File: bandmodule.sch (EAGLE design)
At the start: 15 parts

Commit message: Readme, made more space for toroids
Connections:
- net GND: now also C12.1; no longer C12.2
- net N$6: now also C12.2; no longer C12.1
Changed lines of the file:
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@@
 </segment>
 <segment>
-<pinref part="C12" gate="G$1" pin="2"/>
+<pinref part="C12" gate="G$1" pin="1"/>
 <pinref part="GND8" gate="1" pin="GND"/>
-<wire x1="66.04" y1="22.86" x2="66.04" y2="12.7" width="0.1524" layer="91"/>
+<wire x1="66.04" y1="15.24" x2="66.04" y2="12.7" width="0.1524" layer="91"/>
 </segment>
 </net>
@@
 <segment>
 <pinref part="L7" gate="G$1" pin="1"/>
-<pinref part="C12" gate="G$1" pin="1"/>
+<pinref part="C12" gate="G$1" pin="2"/>
 <wire x1="50.8" y1="27.94" x2="66.04" y2="27.94" width="0.1524" layer="91"/>
 <wire x1="66.04" y1="27.94" x2="66.04" y2="25.4" width="0.1524" layer="91"/>
 <pinref part="TXIN" gate="-2" pin="S"/>
-<wire x1="66.04" y1="25.4" x2="66.04" y2="15.24" width="0.1524" layer="91"/>
+<wire x1="66.04" y1="25.4" x2="66.04" y2="22.86" width="0.1524" layer="91"/>
 <wire x1="66.04" y1="25.4" x2="71.12" y2="25.4" width="0.1524" layer="91"/>
 <junction x="66.04" y="25.4"/>

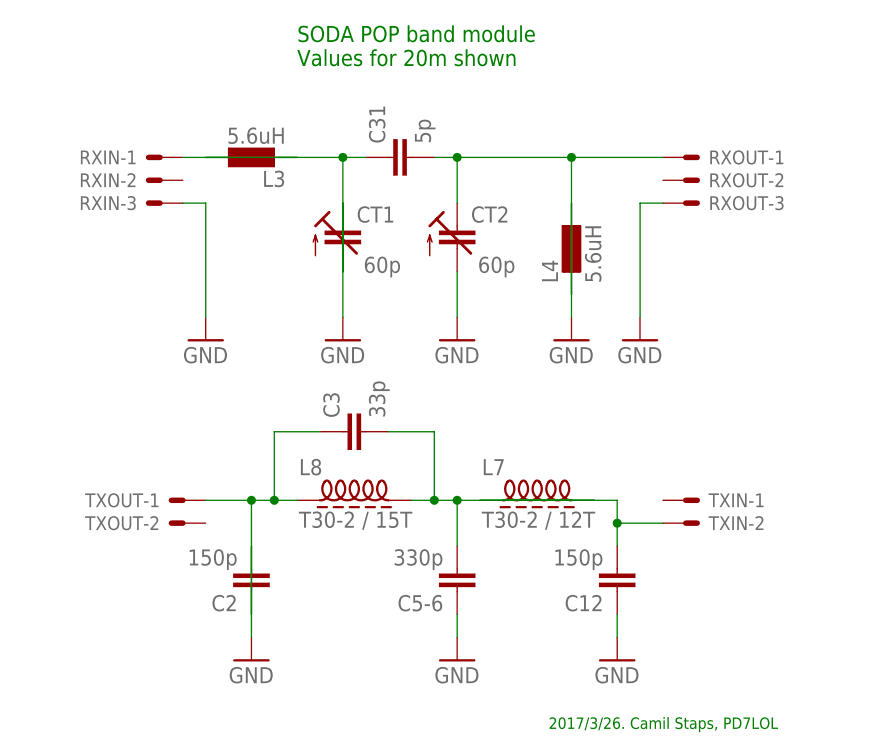
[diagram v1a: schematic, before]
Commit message: Move labels, add white rectangle for band
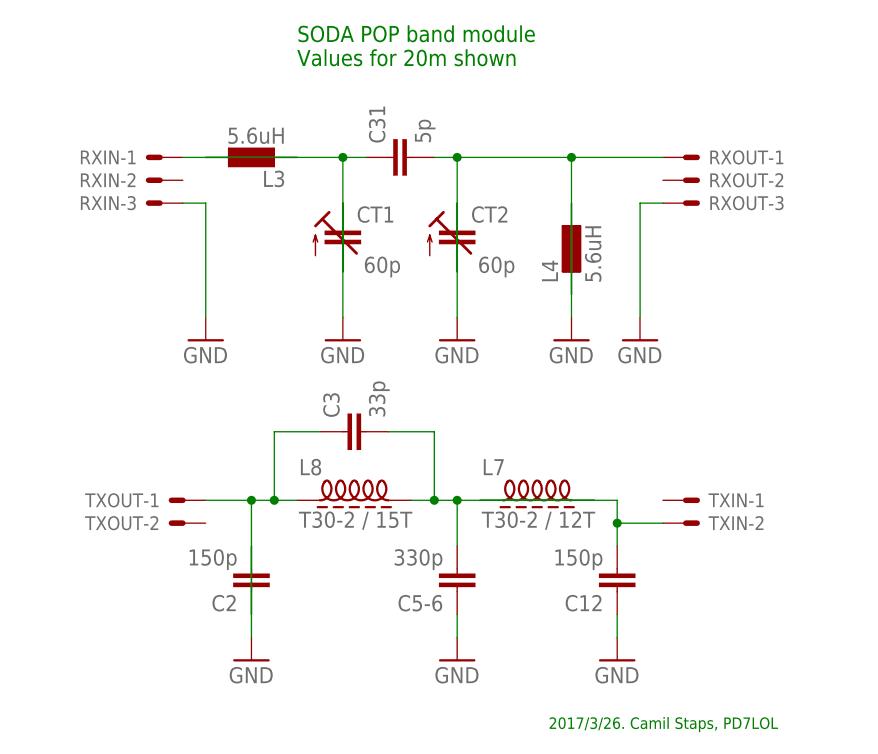
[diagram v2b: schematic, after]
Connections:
- net GND: now also CT2.E; no longer CT2.A
- net N$4: now also CT2.A; no longer CT2.E
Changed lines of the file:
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@@
 <grid distance="0.1" unitdist="inch" unit="inch" style="lines" multiple="1" display="no" altdistance="0.01" altunitdist="inch" altunit="inch"/>
 <layers>
-<layer number="1" name="Top" color="4" fill="10" visible="yes" active="no"/>
-<layer number="16" name="Bottom" color="1" fill="1" visible="yes" active="no"/>
-<layer number="17" name="Pads" color="2" fill="1" visible="yes" active="no"/>
-<layer number="18" name="Vias" color="2" fill="1" visible="yes" active="no"/>
-<layer number="19" name="Unrouted" color="6" fill="1" visible="yes" active="no"/>
-<layer number="20" name="Dimension" color="15" fill="1" visible="yes" active="no"/>
-<layer number="21" name="tPlace" color="7" fill="1" visible="yes" active="no"/>
-<layer number="22" name="bPlace" color="7" fill="1" visible="yes" active="no"/>
-<layer number="23" name="tOrigins" color="15" fill="1" visible="yes" active="no"/>
-<layer number="24" name="bOrigins" color="15" fill="1" visible="yes" active="no"/>
-<layer number="25" name="tNames" color="7" fill="1" visible="yes" active="no"/>
-<layer number="26" name="bNames" color="7" fill="1" visible="yes" active="no"/>
-<layer number="27" name="tValues" color="7" fill="1" visible="yes" active="no"/>
-<layer number="28" name="bValues" color="7" fill="1" visible="yes" active="no"/>
+<layer number="1" name="Top" color="4" fill="10" visible="no" active="no"/>
+<layer number="16" name="Bottom" color="1" fill="1" visible="no" active="no"/>
+<layer number="17" name="Pads" color="2" fill="1" visible="no" active="no"/>
+<layer number="18" name="Vias" color="2" fill="1" visible="no" active="no"/>
+<layer number="19" name="Unrouted" color="6" fill="1" visible="no" active="no"/>
+<layer number="20" name="Dimension" color="15" fill="1" visible="no" active="no"/>
+<layer number="21" name="tPlace" color="7" fill="1" visible="no" active="no"/>
+<layer number="22" name="bPlace" color="7" fill="1" visible="no" active="no"/>
+<layer number="23" name="tOrigins" color="15" fill="1" visible="no" active="no"/>
+<layer number="24" name="bOrigins" color="15" fill="1" visible="no" active="no"/>
+<layer number="25" name="tNames" color="7" fill="1" visible="no" active="no"/>
+<layer number="26" name="bNames" color="7" fill="1" visible="no" active="no"/>
+<layer number="27" name="tValues" color="7" fill="1" visible="no" active="no"/>
+<layer number="28" name="bValues" color="7" fill="1" visible="no" active="no"/>
 <layer number="29" name="tStop" color="7" fill="3" visible="no" active="no"/>
 <layer number="30" name="bStop" color="7" fill="6" visible="no" active="no"/>
@@
 <layer number="35" name="tGlue" color="7" fill="4" visible="no" active="no"/>
 <layer number="36" name="bGlue" color="7" fill="5" visible="no" active="no"/>
-<layer number="37" name="tTest" color="7" fill="1" visible="yes" active="no"/>
-<layer number="38" name="bTest" color="7" fill="1" visible="yes" active="no"/>
+<layer number="37" name="tTest" color="7" fill="1" visible="no" active="no"/>
+<layer number="38" name="bTest" color="7" fill="1" visible="no" active="no"/>
 <layer number="39" name="tKeepout" color="4" fill="11" visible="no" active="no"/>
 <layer number="40" name="bKeepout" color="1" fill="11" visible="no" active="no"/>
@@
 <layer number="44" name="Drills" color="7" fill="1" visible="no" active="no"/>
 <layer number="45" name="Holes" color="7" fill="1" visible="no" active="no"/>
-<layer number="46" name="Milling" color="3" fill="1" visible="yes" active="no"/>
-<layer number="47" name="Measures" color="7" fill="1" visible="yes" active="no"/>
-<layer number="48" name="Document" color="7" fill="1" visible="yes" active="no"/>
-<layer number="49" name="Reference" color="7" fill="1" visible="yes" active="no"/>
-<layer number="51" name="tDocu" color="26" fill="1" visible="yes" active="no"/>
-<layer number="52" name="bDocu" color="7" fill="1" visible="yes" active="no"/>
+<layer number="46" name="Milling" color="3" fill="1" visible="no" active="no"/>
+<layer number="47" name="Measures" color="7" fill="1" visible="no" active="no"/>
+<layer number="48" name="Document" color="7" fill="1" visible="no" active="no"/>
+<layer number="49" name="Reference" color="7" fill="1" visible="no" active="no"/>
+<layer number="51" name="tDocu" color="26" fill="1" visible="no" active="no"/>
+<layer number="52" name="bDocu" color="7" fill="1" visible="no" active="no"/>
 <layer number="90" name="Modules" color="5" fill="1" visible="yes" active="yes"/>
 <layer number="91" name="Nets" color="2" fill="1" visible="yes" active="yes"/>
@@
 <pinref part="C31" gate="G$1" pin="2"/>
 <wire x1="45.72" y1="66.04" x2="48.26" y2="66.04" width="0.1524" layer="91"/>
-<pinref part="CT2" gate="G$1" pin="E"/>
+<pinref part="CT2" gate="G$1" pin="A"/>
 <wire x1="48.26" y1="66.04" x2="60.96" y2="66.04" width="0.1524" layer="91"/>
-<wire x1="48.26" y1="66.04" x2="48.26" y2="60.96" width="0.1524" layer="91"/>
+<wire x1="48.26" y1="66.04" x2="48.26" y2="53.34" width="0.1524" layer="91"/>
 <junction x="48.26" y="66.04"/>
 <junction x="60.96" y="66.04"/>
@@
 </segment>
 <segment>
-<pinref part="CT2" gate="G$1" pin="A"/>
+<pinref part="CT2" gate="G$1" pin="E"/>
 <pinref part="GND4" gate="1" pin="GND"/>
-<wire x1="48.26" y1="53.34" x2="48.26" y2="48.26" width="0.1524" layer="91"/>
+<wire x1="48.26" y1="60.96" x2="48.26" y2="48.26" width="0.1524" layer="91"/>
 </segment>
 <segment>

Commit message: Split up C5-6
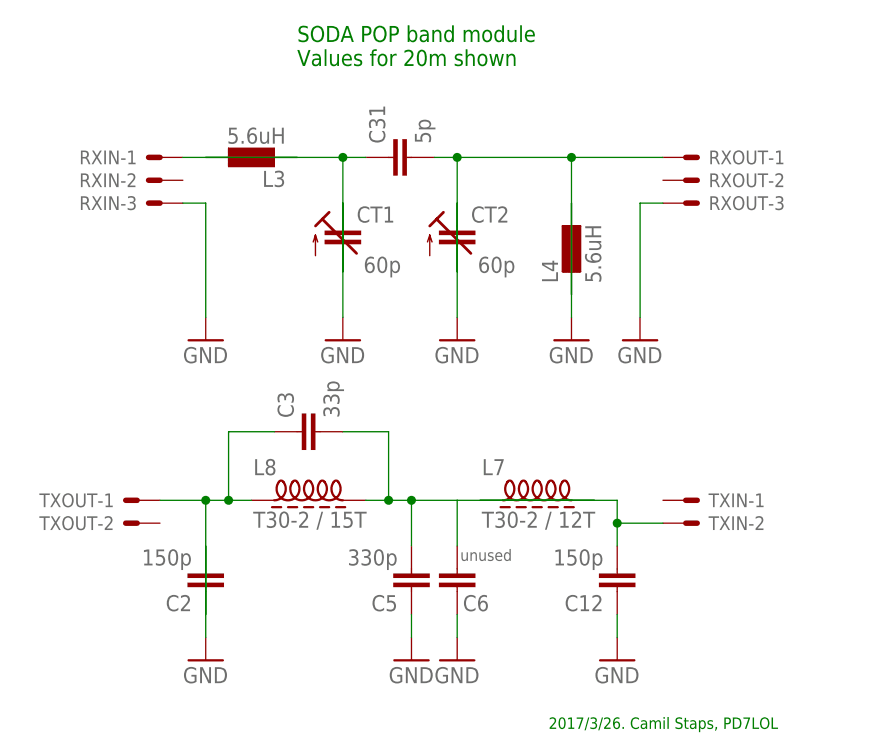
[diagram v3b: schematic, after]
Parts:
- added C5: 330p, capacitor-wima:C5/2.5
- C6: value 330p -> unused
- renumbered C5-6 to C6
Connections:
- net GND: now also C5.1
- net N$5: now also C5.2
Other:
- moved on the sheet: C2, C3, L8, TXOUT-1, TXOUT-2
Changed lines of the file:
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@@
 <part name="L8" library="toroids" deviceset="INDUCTOR" device="T30-2-28AWG-12T" value="T30-2 / 15T"/>
 <part name="L7" library="toroids" deviceset="INDUCTOR" device="T30-2-28AWG-12T" value="T30-2 / 12T"/>
-<part name="C5-6" library="capacitor-wima" deviceset="C" device="5/2.5" value="330p"/>
+<part name="C5" library="capacitor-wima" deviceset="C" device="5/2.5" value="330p"/>
 <part name="C12" library="capacitor-wima" deviceset="C" device="5/2.5" value="150p"/>
 <part name="C3" library="capacitor-wima" deviceset="C" device="5/2.5" value="33p"/>
@@
 <part name="L4" library="eagle-ltspice" deviceset="L" device="0207/10" value="5.6uH"/>
 <part name="L3" library="eagle-ltspice" deviceset="L" device="0207/10" value="5.6uH"/>
+<part name="C6" library="capacitor-wima" deviceset="C" device="5/2.5" value="unused"/>
+<part name="GND9" library="supply1" deviceset="GND" device=""/>
 </parts>
 <sheets>
@@
 </instance>
 <instance part="TXIN" gate="-2" x="73.66" y="25.4"/>
-<instance part="TXOUT" gate="-1" x="17.78" y="27.94" smashed="yes" rot="MR0">
-<attribute name="NAME" x="15.24" y="27.178" size="1.524" layer="95" rot="MR0"/>
-</instance>
-<instance part="TXOUT" gate="-2" x="17.78" y="25.4" rot="MR0"/>
-<instance part="C2" gate="G$1" x="25.4" y="17.78" rot="R180"/>
-<instance part="L8" gate="G$1" x="35.56" y="27.94"/>
+<instance part="TXOUT" gate="-1" x="12.7" y="27.94" smashed="yes" rot="MR0">
+<attribute name="NAME" x="10.16" y="27.178" size="1.524" layer="95" rot="MR0"/>
+</instance>
+<instance part="TXOUT" gate="-2" x="12.7" y="25.4" rot="MR0"/>
+<instance part="C2" gate="G$1" x="20.32" y="17.78" rot="R180"/>
+<instance part="L8" gate="G$1" x="30.48" y="27.94"/>
 <instance part="L7" gate="G$1" x="55.88" y="27.94"/>
-<instance part="C5-6" gate="G$1" x="48.26" y="17.78" rot="R180"/>
+<instance part="C5" gate="G$1" x="43.18" y="17.78" smashed="yes" rot="R180">
+<attribute name="NAME" x="41.656" y="17.399" size="1.778" layer="95" rot="R180"/>
+<attribute name="VALUE" x="41.656" y="22.479" size="1.778" layer="96" rot="R180"/>
+</instance>
 <instance part="C12" gate="G$1" x="66.04" y="17.78" rot="R180"/>
-<instance part="C3" gate="G$1" x="35.56" y="35.56" rot="R90"/>
-<instance part="GND6" gate="1" x="25.4" y="10.16"/>
-<instance part="GND7" gate="1" x="48.26" y="10.16"/>
+<instance part="C3" gate="G$1" x="30.48" y="35.56" rot="R90"/>
+<instance part="GND6" gate="1" x="20.32" y="10.16"/>
+<instance part="GND7" gate="1" x="43.18" y="10.16"/>
 <instance part="GND8" gate="1" x="66.04" y="10.16"/>
 <instance part="L4" gate="G$1" x="60.96" y="55.88"/>
 <instance part="L3" gate="G$1" x="25.4" y="66.04" rot="R90"/>
+<instance part="C6" gate="G$1" x="48.26" y="17.78" smashed="yes" rot="R180">
+<attribute name="NAME" x="51.816" y="17.399" size="1.778" layer="95" rot="R180"/>
+<attribute name="VALUE" x="54.356" y="22.479" size="1.27" layer="96" rot="R180"/>
+</instance>
+<instance part="GND9" gate="1" x="48.26" y="10.16"/>
 </instances>
 <busses>
@@
 <pinref part="C2" gate="G$1" pin="2"/>
 <pinref part="GND6" gate="1" pin="GND"/>
-<wire x1="25.4" y1="22.86" x2="25.4" y2="12.7" width="0.1524" layer="91"/>
-</segment>
-<segment>
-<pinref part="C5-6" gate="G$1" pin="1"/>
+<wire x1="20.32" y1="22.86" x2="20.32" y2="12.7" width="0.1524" layer="91"/>
+</segment>
+<segment>
+<pinref part="C5" gate="G$1" pin="1"/>
 <pinref part="GND7" gate="1" pin="GND"/>
-<wire x1="48.26" y1="15.24" x2="48.26" y2="12.7" width="0.1524" layer="91"/>
+<wire x1="43.18" y1="15.24" x2="43.18" y2="12.7" width="0.1524" layer="91"/>
 </segment>
 <segment>
@@
 <pinref part="GND8" gate="1" pin="GND"/>
 <wire x1="66.04" y1="15.24" x2="66.04" y2="12.7" width="0.1524" layer="91"/>
+</segment>
+<segment>
+<pinref part="GND9" gate="1" pin="GND"/>
+<pinref part="C6" gate="G$1" pin="1"/>
+<wire x1="48.26" y1="12.7" x2="48.26" y2="15.24" width="0.1524" layer="91"/>
 </segment>
 </net>
@@
 <pinref part="L8" gate="G$1" pin="2"/>
 <pinref part="L7" gate="G$1" pin="2"/>
-<wire x1="43.18" y1="27.94" x2="45.72" y2="27.94" width="0.1524" layer="91"/>
-<pinref part="C5-6" gate="G$1" pin="2"/>
-<wire x1="45.72" y1="27.94" x2="48.26" y2="27.94" width="0.1524" layer="91"/>
+<wire x1="38.1" y1="27.94" x2="40.64" y2="27.94" width="0.1524" layer="91"/>
+<pinref part="C5" gate="G$1" pin="2"/>
+<wire x1="40.64" y1="27.94" x2="43.18" y2="27.94" width="0.1524" layer="91"/>
+<wire x1="43.18" y1="27.94" x2="48.26" y2="27.94" width="0.1524" layer="91"/>
 <wire x1="48.26" y1="27.94" x2="63.5" y2="27.94" width="0.1524" layer="91"/>
-<wire x1="48.26" y1="27.94" x2="48.26" y2="22.86" width="0.1524" layer="91"/>
+<wire x1="43.18" y1="27.94" x2="43.18" y2="22.86" width="0.1524" layer="91"/>
 <pinref part="C3" gate="G$1" pin="2"/>
-<wire x1="40.64" y1="35.56" x2="45.72" y2="35.56" width="0.1524" layer="91"/>
-<wire x1="45.72" y1="35.56" x2="45.72" y2="27.94" width="0.1524" layer="91"/>
-<junction x="45.72" y="27.94"/>
-<junction x="48.26" y="27.94"/>
+<wire x1="35.56" y1="35.56" x2="40.64" y2="35.56" width="0.1524" layer="91"/>
+<wire x1="40.64" y1="35.56" x2="40.64" y2="27.94" width="0.1524" layer="91"/>
+<junction x="40.64" y="27.94"/>
+<junction x="43.18" y="27.94"/>
+<pinref part="C6" gate="G$1" pin="2"/>
+<wire x1="48.26" y1="22.86" x2="48.26" y2="27.94" width="0.1524" layer="91"/>
 </segment>
 </net>
@@
 <segment>
 <pinref part="C3" gate="G$1" pin="1"/>
-<wire x1="27.94" y1="35.56" x2="33.02" y2="35.56" width="0.1524" layer="91"/>
+<wire x1="22.86" y1="35.56" x2="27.94" y2="35.56" width="0.1524" layer="91"/>
 <pinref part="TXOUT" gate="-1" pin="S"/>
 <pinref part="L8" gate="G$1" pin="1"/>
-<wire x1="20.32" y1="27.94" x2="25.4" y2="27.94" width="0.1524" layer="91"/>
+<wire x1="15.24" y1="27.94" x2="20.32" y2="27.94" width="0.1524" layer="91"/>
 <pinref part="C2" gate="G$1" pin="1"/>
-<wire x1="25.4" y1="27.94" x2="27.94" y2="27.94" width="0.1524" layer="91"/>
-<wire x1="27.94" y1="27.94" x2="30.48" y2="27.94" width="0.1524" layer="91"/>
-<wire x1="25.4" y1="27.94" x2="25.4" y2="15.24" width="0.1524" layer="91"/>
-<wire x1="27.94" y1="35.56" x2="27.94" y2="27.94" width="0.1524" layer="91"/>
-<junction x="25.4" y="27.94"/>
-<junction x="27.94" y="27.94"/>
-</segment>
-</net>
+<wire x1="20.32" y1="27.94" x2="22.86" y2="27.94" width="0.1524" layer="91"/>
+<wire x1="22.86" y1="27.94" x2="25.4" y2="27.94" width="0.1524" layer="91"/>
+<wire x1="20.32" y1="27.94" x2="20.32" y2="15.24" width="0.1524" layer="91"/>
+<wire x1="22.86" y1="35.56" x2="22.86" y2="27.94" width="0.1524" layer="91"/>
+<junction x="20.32" y="27.94"/>
+<junction x="22.86" y="27.94"/>
+</segment>
+</net>

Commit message: Move RX around for larger board note rectangle
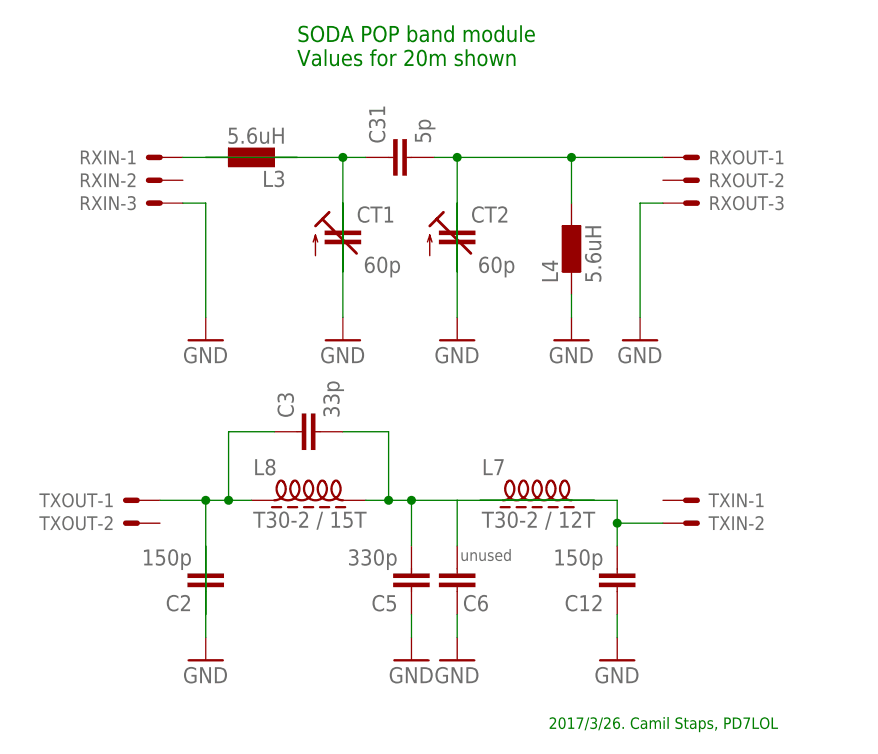
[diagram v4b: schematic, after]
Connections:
- net GND: now also L4.2; no longer L4.1
- net N$4: now also L4.1; no longer L4.2
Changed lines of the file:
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@@
 <junction x="48.26" y="66.04"/>
 <junction x="60.96" y="66.04"/>
-<pinref part="L4" gate="G$1" pin="2"/>
-<wire x1="60.96" y1="50.8" x2="60.96" y2="66.04" width="0.1524" layer="91"/>
+<pinref part="L4" gate="G$1" pin="1"/>
+<wire x1="60.96" y1="60.96" x2="60.96" y2="66.04" width="0.1524" layer="91"/>
 </segment>
 </net>
@@
 <segment>
 <pinref part="GND5" gate="1" pin="GND"/>
-<wire x1="60.96" y1="60.96" x2="60.96" y2="48.26" width="0.1524" layer="91"/>
-<pinref part="L4" gate="G$1" pin="1"/>
+<wire x1="60.96" y1="50.8" x2="60.96" y2="48.26" width="0.1524" layer="91"/>
+<pinref part="L4" gate="G$1" pin="2"/>
 </segment>
 <segment>
